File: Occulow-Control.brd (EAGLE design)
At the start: 38.1 x 101.6 mm, 40 parts, among them J1 CORTEX_DEBUG_PTH, T1 DMP3010LK3, T2 DMP3010LK3, T3 DMP3010LK3

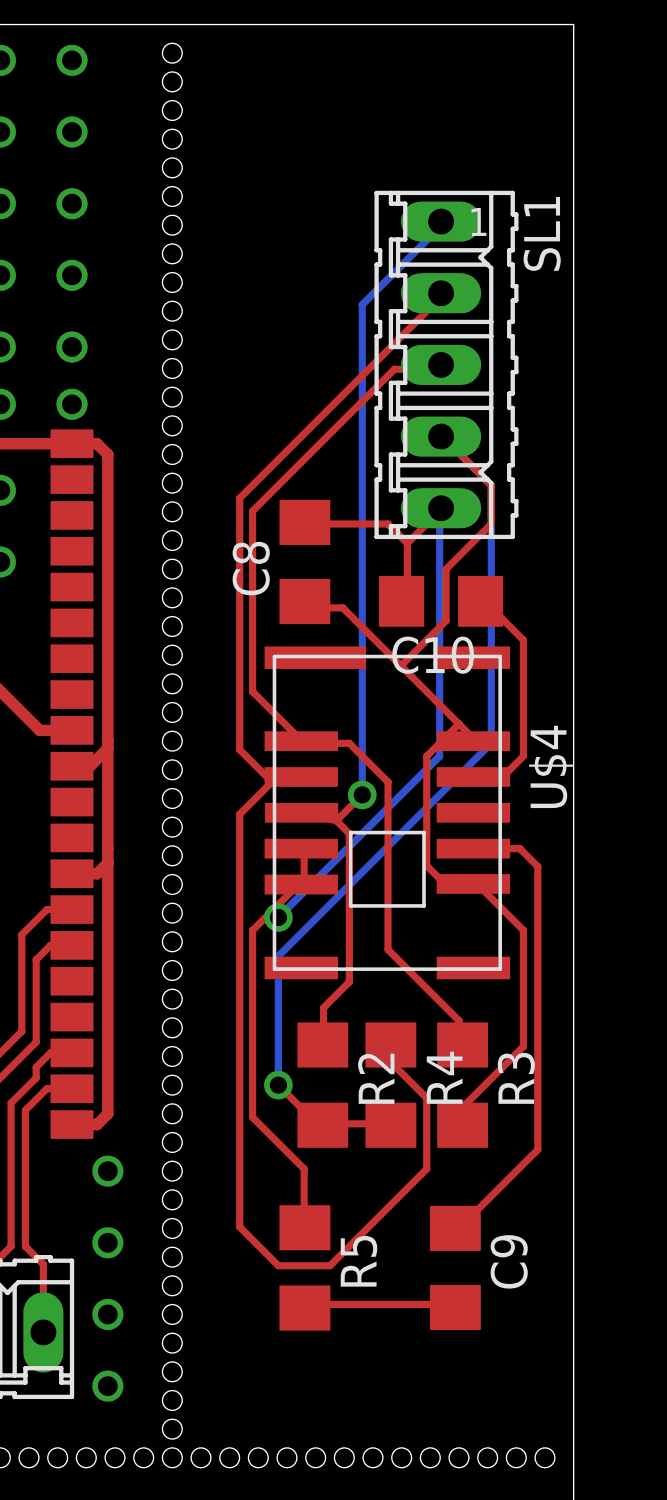
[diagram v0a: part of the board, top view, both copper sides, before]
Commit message: Attempted to slim down grideye board
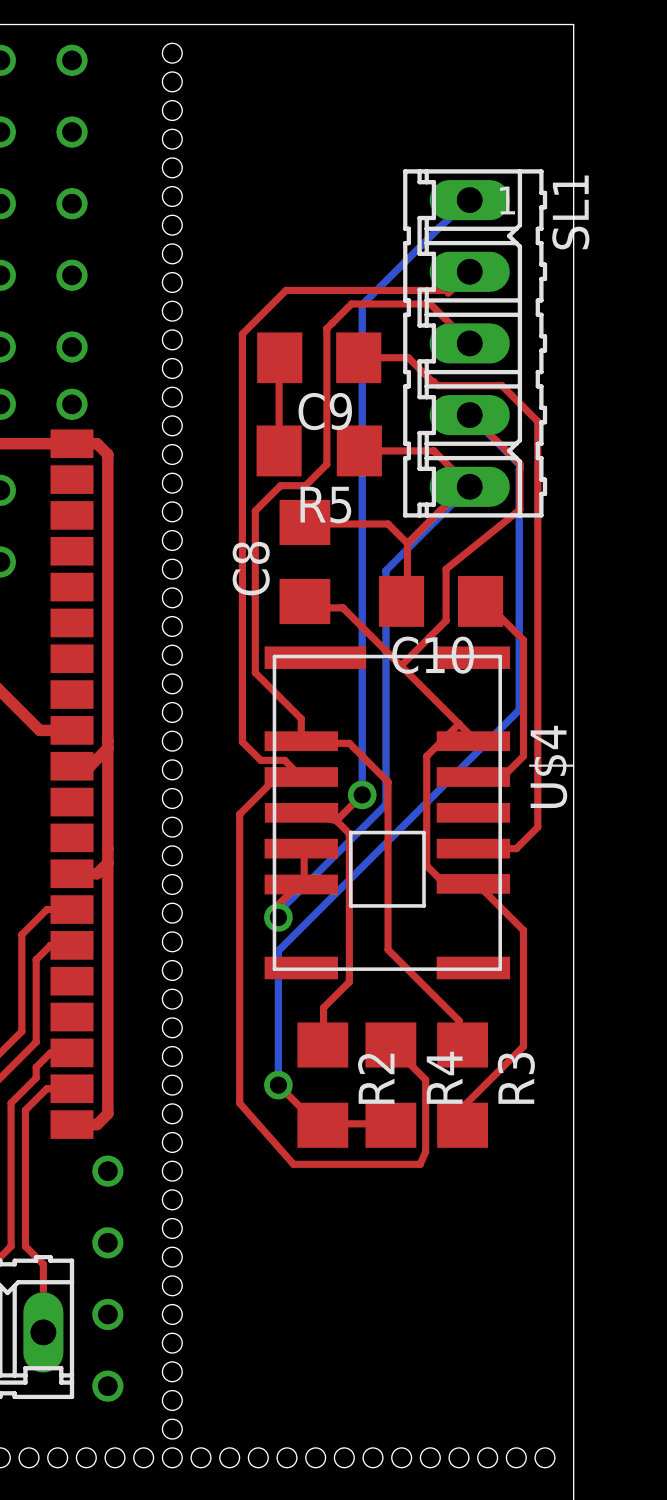
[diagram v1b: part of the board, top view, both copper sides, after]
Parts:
- moved C9 32.6 mm to (29.1, 89.8), turned to 180 degrees
- moved R5 29.0 mm to (29.1, 86.5), turned to 180 degrees
- moved SL1 1.27 mm to (34.4, 90.3)
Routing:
- net N$2: track 16.7 -> 24.3 mm
- net GR_SDA: track 31.8 -> 37.2 mm
- net GR_GND: track 40.1 -> 36.1 mm
- net GR_VCC: track 67.5 -> 70.6 mm
- net N$3: track 5.41 -> 3.31 mm
- net GR_INT: track 33.9 -> 35.1 mm
- net GR_SCL: track 52.7 -> 53.3 mm

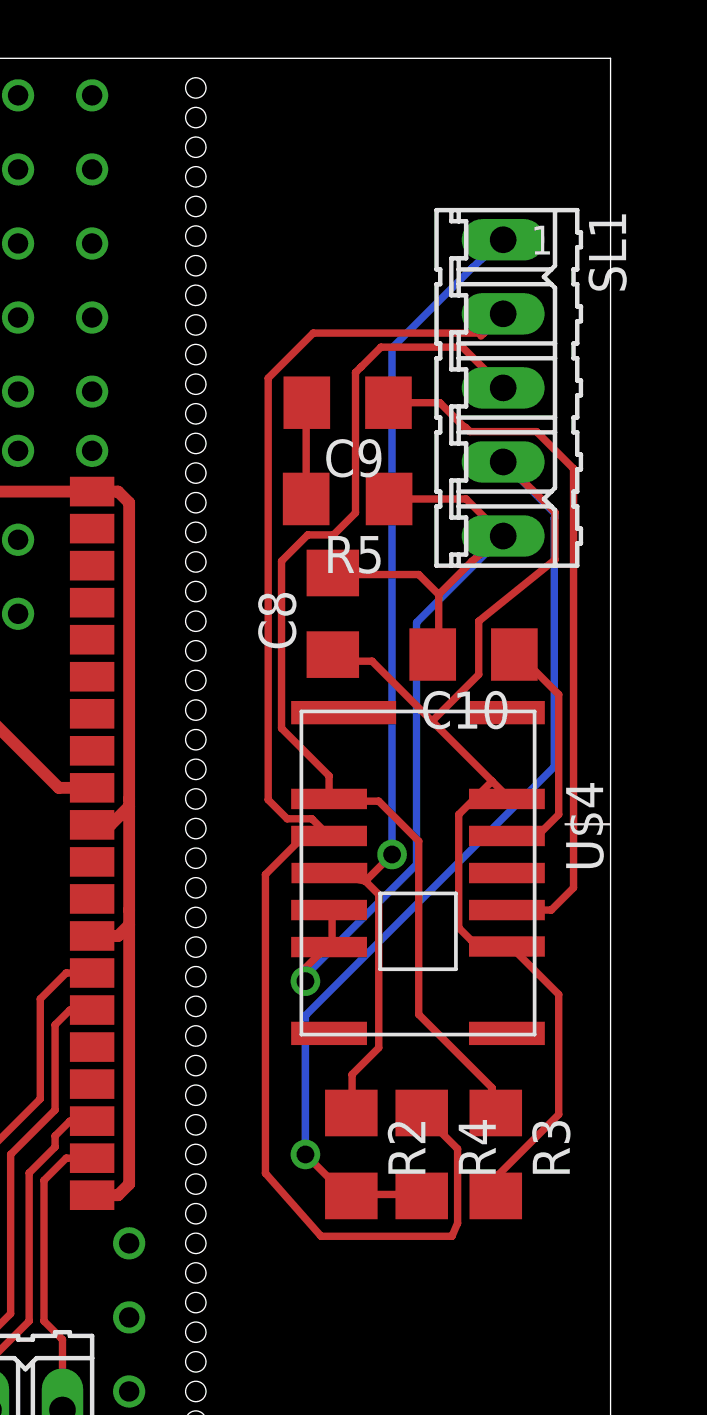
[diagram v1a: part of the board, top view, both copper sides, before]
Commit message: Moved grideye to the top, added more perforation holes
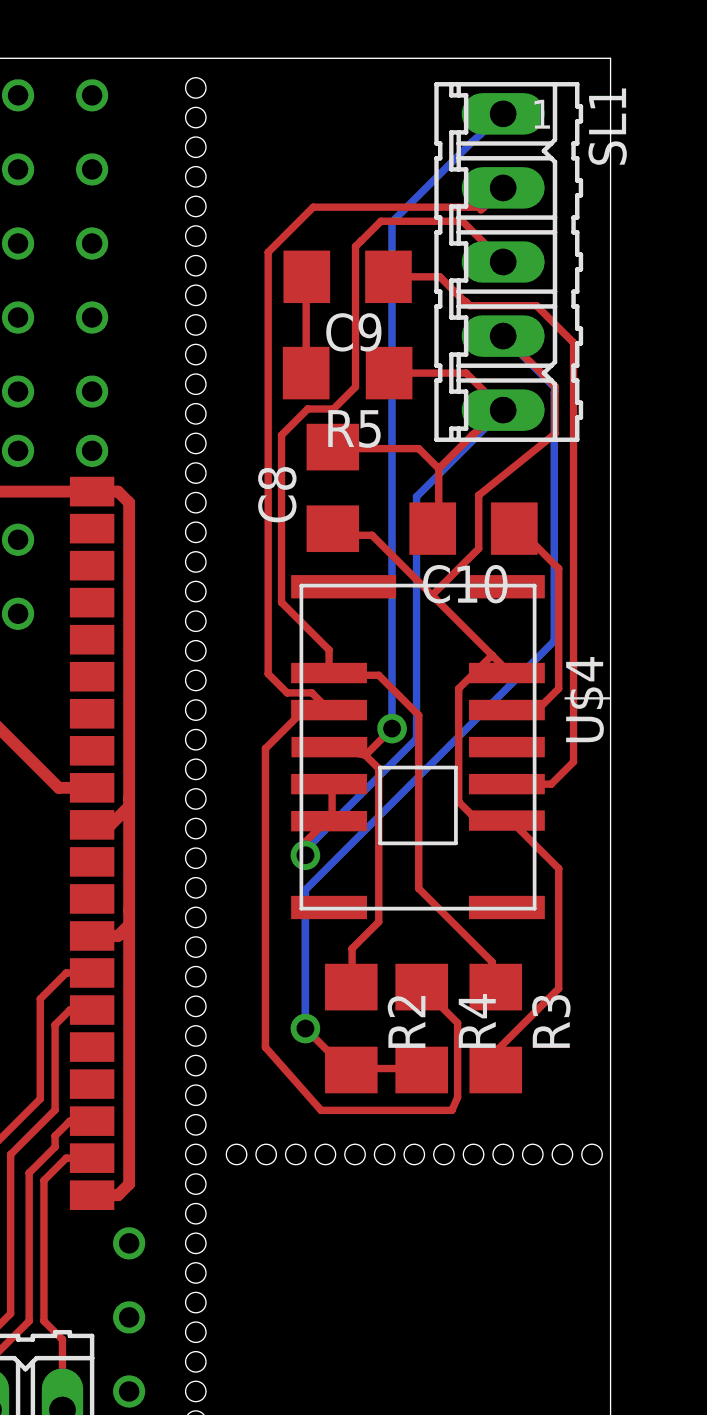
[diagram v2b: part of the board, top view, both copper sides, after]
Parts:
- moved R5 4.32 mm to (29.1, 90.8)
- moved C10 4.32 mm to (33.4, 85.5)
- moved C8 4.32 mm to (28.6, 86.9)
- moved C9 4.32 mm to (29.1, 94.1)
- moved R2 4.32 mm to (29.2, 68.3)
- moved R3 4.32 mm to (34.2, 68.3)
- moved R4 4.32 mm to (31.6, 68.3)
- moved SL1 4.32 mm to (34.4, 94.6)
- moved U$4 4.32 mm to (31.5, 78.0)

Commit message: Ground plane
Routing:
- net LR_GND: track 119.3 -> 1.36 mm, vias 0 -> 53
- added copper zone on layer 1, net LR_GND
- added copper zone on layer 16, net LR_GND

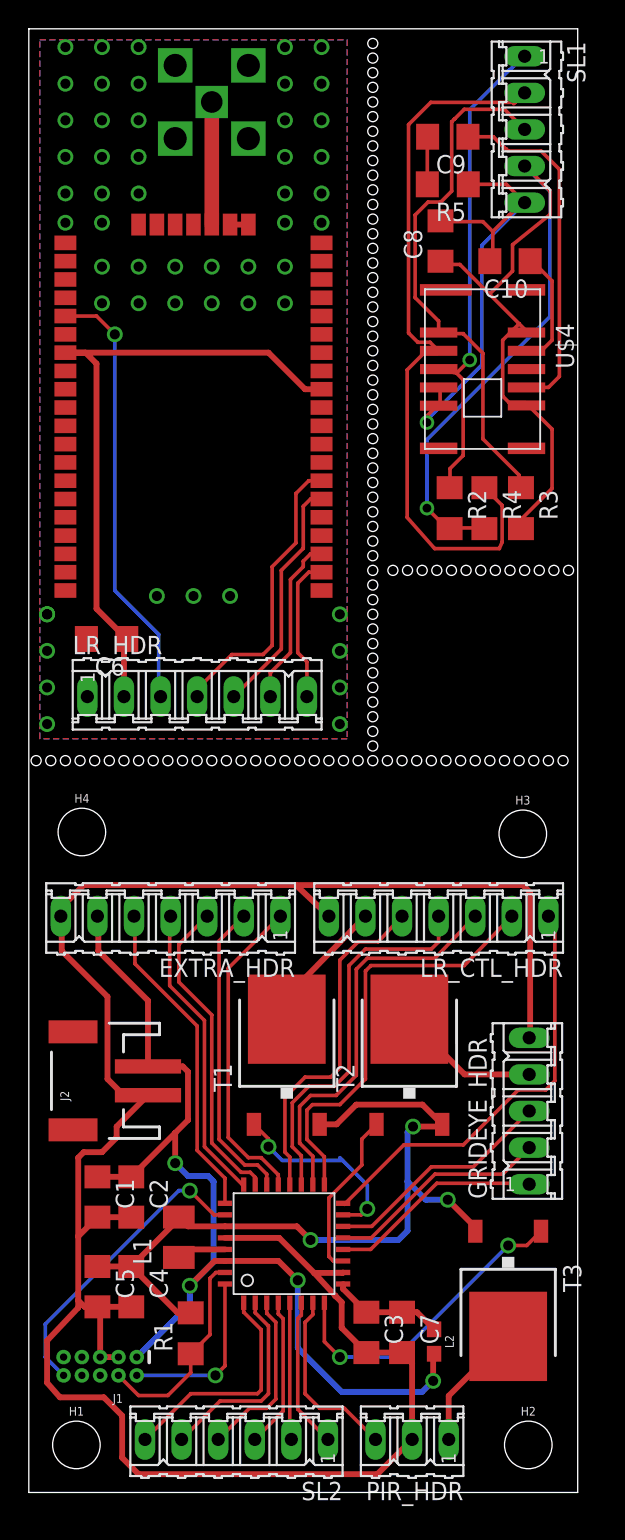
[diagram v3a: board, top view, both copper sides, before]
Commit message: Labels for most headers, moved some ground vias
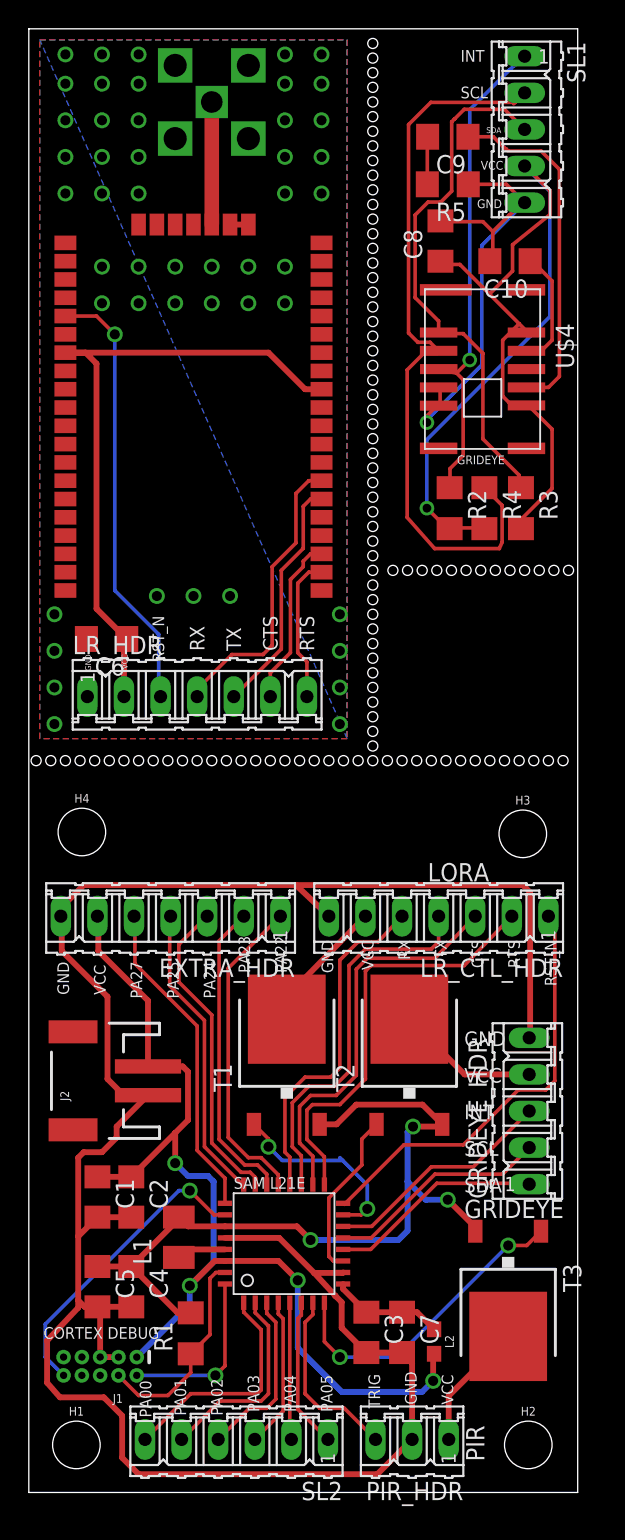
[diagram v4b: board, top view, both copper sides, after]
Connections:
- net LR_GND renamed N!!
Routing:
- net N!!: vias 53 -> 48
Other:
- board text added: "CORTEX DEBUG"
- board text added: "CTS"
- board text added: "GND"
- board text added: "GRIDEYE"
- board text added: "INT"
- board text added: "LORA"
- board text added: "PA00"
- board text added: "PA01"
- board text added: "PA02"
- board text added: "PA03"
- board text added: "PA04"
- board text added: "PA05"
- board text added: "PA22"
- board text added: "PA23"
- board text added: "PA24"
- board text added: "PA25"
- board text added: "PA27"
- board text added: "PIR"
- board text added: "RST_N"
- board text added: "RTS"
- board text added: "RX"
- board text added: "SAM L21E"
- board text added: "SCL"
- board text added: "SDA"
- board text added: "TRIG"
- board text added: "TX"
- board text added: "VCC"
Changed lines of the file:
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@@
 <?xml version="1.0" encoding="utf-8"?>
 <!DOCTYPE eagle SYSTEM "eagle.dtd">
-<eagle version="8.1.0">
+<eagle version="8.0.2">
 <drawing>
 <settings>
@@
 <hole x="36.449" y="64.008" drill="0.7"/>
 <hole x="37.465" y="64.008" drill="0.7"/>
+<text x="30.226" y="30.988" size="1.016" layer="21">GND</text>
+<text x="30.226" y="28.448" size="1.016" layer="21">VCC</text>
+<text x="30.226" y="25.908" size="1.016" layer="21">INT</text>
+<text x="30.226" y="23.368" size="1.016" layer="21">SCL</text>
+<text x="30.226" y="20.828" size="1.016" layer="21">SDA</text>
+<text x="30.226" y="19.05" size="1.27" layer="21">GRIDEYE</text>
+<text x="24.384" y="5.842" size="0.8128" layer="21" rot="R90">TRIG</text>
+<text x="26.924" y="6.096" size="0.8128" layer="21" rot="R90">GND</text>
+<text x="29.464" y="6.096" size="0.8128" layer="21" rot="R90">VCC</text>
+<text x="31.623" y="2.159" size="1.27" layer="21" rot="R90">PIR</text>
+<text x="8.509" y="5.207" size="0.8128" layer="21" rot="R90">PA00</text>
+<text x="10.922" y="5.334" size="0.8128" layer="21" rot="R90">PA01</text>
+<text x="13.462" y="5.334" size="0.8128" layer="21" rot="R90">PA02</text>
+<text x="16.002" y="5.588" size="0.8128" layer="21" rot="R90">PA03</text>
+<text x="18.542" y="5.588" size="0.8128" layer="21" rot="R90">PA04</text>
+<text x="21.082" y="5.588" size="0.8128" layer="21" rot="R90">PA05</text>
+<text x="1.016" y="10.668" size="0.8128" layer="21">CORTEX DEBUG</text>
+<text x="20.32" y="38.354" size="0.8128" layer="21" rot="R270">GND</text>
+<text x="23.114" y="38.354" size="0.8128" layer="21" rot="R270">VCC</text>
+<text x="25.654" y="38.354" size="0.8128" layer="21" rot="R270">RX</text>
+<text x="28.194" y="38.354" size="0.8128" layer="21" rot="R270">TX</text>
+<text x="30.734" y="38.354" size="0.8128" layer="21" rot="R270">CTS</text>
+<text x="33.274" y="38.354" size="0.8128" layer="21" rot="R270">RTS</text>
+<text x="35.814" y="38.354" size="0.8128" layer="21" rot="R270">RST_N</text>
+<text x="27.686" y="42.418" size="1.27" layer="21">LORA</text>
+<text x="2.794" y="34.544" size="0.8128" layer="21" rot="R90">GND</text>
+<text x="5.334" y="34.544" size="0.8128" layer="21" rot="R90">VCC</text>
+<text x="7.874" y="34.29" size="0.8128" layer="21" rot="R90">PA27</text>
+<text x="10.414" y="34.29" size="0.8128" layer="21" rot="R90">PA25</text>
+<text x="12.954" y="34.29" size="0.8128" layer="21" rot="R90">PA24</text>
+<text x="15.367" y="36.068" size="0.8128" layer="21" rot="R90">PA23</text>
+<text x="17.907" y="36.068" size="0.8128" layer="21" rot="R90">PA22</text>
+<text x="14.224" y="21.082" size="0.8128" layer="21">SAM L21E</text>
+<text x="29.972" y="99.314" size="0.8128" layer="21">INT</text>
+<text x="29.972" y="96.774" size="0.8128" layer="21">SCL</text>
+<text x="31.75" y="94.361" size="0.4064" layer="21">SDA</text>
+<text x="31.369" y="91.821" size="0.6096" layer="21">VCC</text>
+<text x="31.115" y="89.154" size="0.6096" layer="21">GND</text>
+<text x="29.718" y="71.374" size="0.6096" layer="21">GRIDEYE</text>
+<text x="19.812" y="58.42" size="1.016" layer="21" rot="R90">RTS</text>
+<text x="17.272" y="58.42" size="1.016" layer="21" rot="R90">CTS</text>
+<text x="14.732" y="58.42" size="1.016" layer="21" rot="R90">TX</text>
+<text x="12.192" y="58.42" size="1.016" layer="21" rot="R90">RX</text>
+<text x="9.398" y="57.658" size="0.8128" layer="21" rot="R90">RST_N</text>
+<text x="6.858" y="57.15" size="0.4064" layer="21" rot="R90">VCC</text>
+<text x="4.318" y="57.023" size="0.4064" layer="21" rot="R90">GND</text>
 </plain>
 <attributes>
@@
 <wire x1="17.907" y1="34.417" x2="23.368" y2="40.005" width="0.4064" layer="1"/>
 </signal>
-<signal name="LR_GND">
+<signal name="N!!">
 <contactref element="U$2" pad="33"/>
 <contactref element="U$2" pad="41"/>
@@
 <vertex x="0.762" y="52.324"/>
 </polygon>
-<via x="2.54" y="100.33" extent="1-16" drill="0.7"/>
-<via x="7.62" y="100.33" extent="1-16" drill="0.7"/>
-<via x="5.08" y="100.33" extent="1-16" drill="0.7"/>
-<via x="17.78" y="100.33" extent="1-16" drill="0.7"/>
-<via x="20.32" y="100.33" extent="1-16" drill="0.7"/>
+<via x="2.54" y="99.822" extent="1-16" drill="0.7"/>
+<via x="7.62" y="99.822" extent="1-16" drill="0.7"/>
+<via x="5.08" y="99.822" extent="1-16" drill="0.7"/>
+<via x="17.78" y="99.822" extent="1-16" drill="0.7"/>
+<via x="20.32" y="99.822" extent="1-16" drill="0.7"/>
 <via x="20.32" y="97.79" extent="1-16" drill="0.7"/>
 <via x="17.78" y="97.79" extent="1-16" drill="0.7"/>
@@
 <via x="17.78" y="90.17" extent="1-16" drill="0.7"/>
 <via x="20.32" y="90.17" extent="1-16" drill="0.7"/>
-<via x="20.32" y="88.138" extent="1-16" drill="0.7"/>
-<via x="17.78" y="88.138" extent="1-16" drill="0.7"/>
 <via x="7.62" y="92.71" extent="1-16" drill="0.7"/>
 <via x="5.08" y="92.71" extent="1-16" drill="0.7"/>
@@
 <via x="5.08" y="90.17" extent="1-16" drill="0.7"/>
 <via x="7.62" y="90.17" extent="1-16" drill="0.7"/>
-<via x="5.08" y="88.138" extent="1-16" drill="0.7"/>
-<via x="2.54" y="88.138" extent="1-16" drill="0.7"/>
 <via x="5.08" y="85.09" extent="1-16" drill="0.7"/>
 <via x="7.62" y="85.09" extent="1-16" drill="0.7"/>
@@
 <via x="7.62" y="82.55" extent="1-16" drill="0.7"/>
 <via x="5.08" y="82.55" extent="1-16" drill="0.7"/>
-<via x="1.27" y="60.96" extent="1-16" drill="0.7"/>
-<via x="1.27" y="58.42" extent="1-16" drill="0.7"/>
-<via x="1.27" y="55.88" extent="1-16" drill="0.7"/>
-<via x="1.27" y="53.34" extent="1-16" drill="0.7"/>
+<via x="1.778" y="60.96" extent="1-16" drill="0.7"/>
+<via x="1.778" y="58.42" extent="1-16" drill="0.7"/>
+<via x="1.778" y="55.88" extent="1-16" drill="0.7"/>
+<via x="1.778" y="53.34" extent="1-16" drill="0.7"/>
 <via x="21.59" y="60.96" extent="1-16" drill="0.7"/>
 <via x="21.59" y="58.42" extent="1-16" drill="0.7"/>
 <via x="21.59" y="55.88" extent="1-16" drill="0.7"/>
 <via x="21.59" y="53.34" extent="1-16" drill="0.7"/>
-<wire x1="21.59" y1="55.88" x2="21.59" y2="53.34" width="0" layer="19" extent="1-1"/>
 <polygon width="0.4064" layer="16" isolate="0.3048">
 <vertex x="0.762" y="100.838"/>
 <vertex x="22.098" y="100.838"/>
 <vertex x="22.098" y="52.324"/>
-<vertex x="0.762" y="52.324"/>
 </polygon>
-<via x="1.27" y="60.96" extent="1-16" drill="0.7"/>
 <via x="8.89" y="62.23" extent="1-16" drill="0.7"/>
 <via x="11.43" y="62.23" extent="1-16" drill="0.7"/>
